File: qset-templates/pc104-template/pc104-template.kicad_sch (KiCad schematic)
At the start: 8 parts

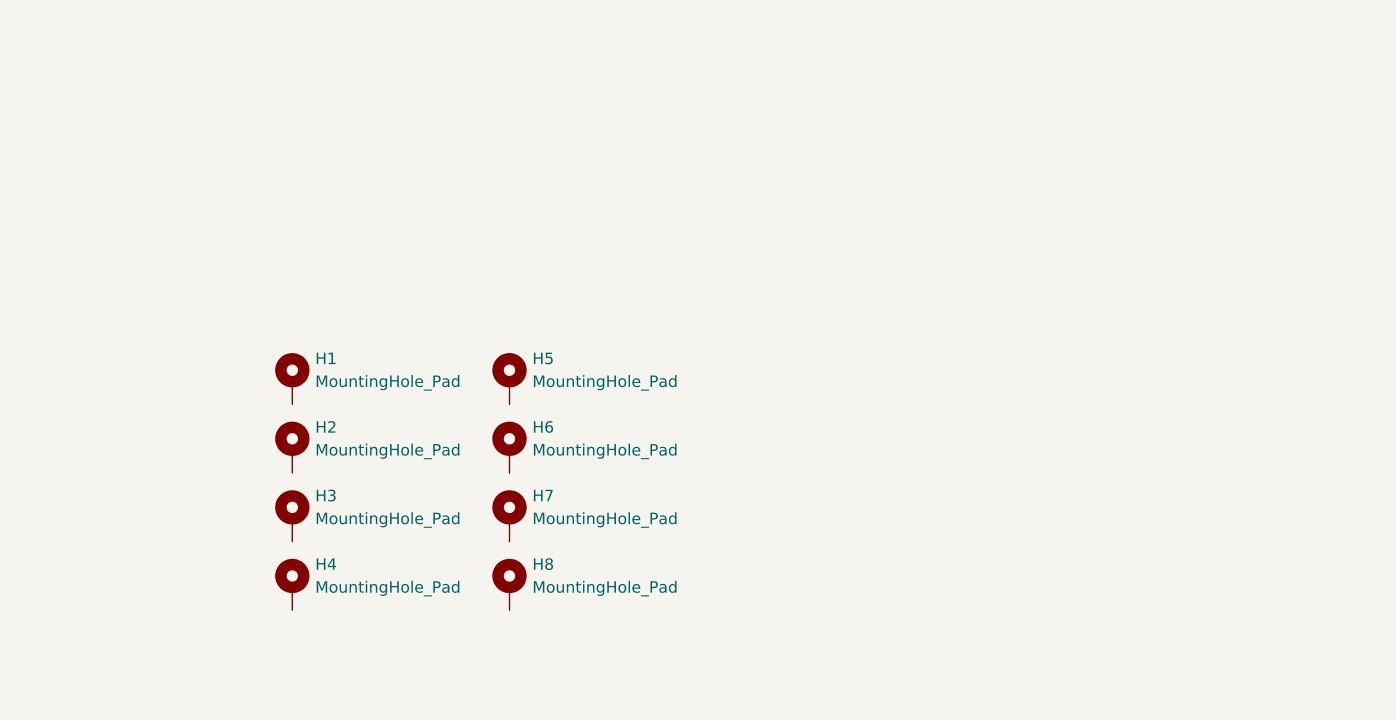
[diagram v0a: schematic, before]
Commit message: templates: pc104: complete template with MH, PC104, and edges
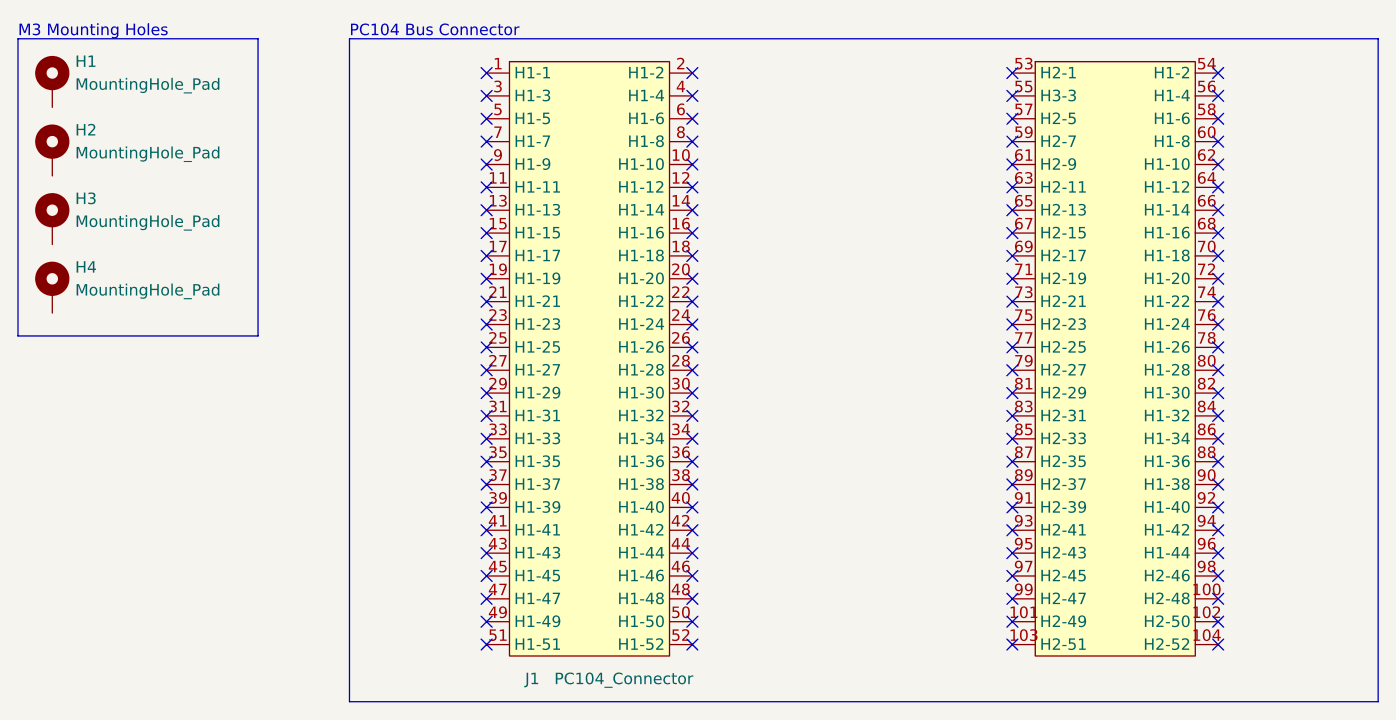
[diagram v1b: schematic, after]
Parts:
- removed H5, H6, H7, H8: MountingHole_Pad, MountingHole:MountingHole_3.2mm_M3_Pad_TopBottom, symbol Mechanical:MountingHole_Pad
- added J1: PC104_Connector, pc104-connector:pc104-connector, symbol qset-connector-library:PC104_Connector
- H1: footprint (none) -> MountingHole:MountingHole_3.2mm_M3_Pad_TopBottom
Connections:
- no-connect marks 0 -> 104
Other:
- note added: "M3 Mounting Holes"
- note added: "PC104 Bus Connector"
- moved on the sheet: H1, H2, H3, H4

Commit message: templates: pc104: include cutouts on all 4 edges
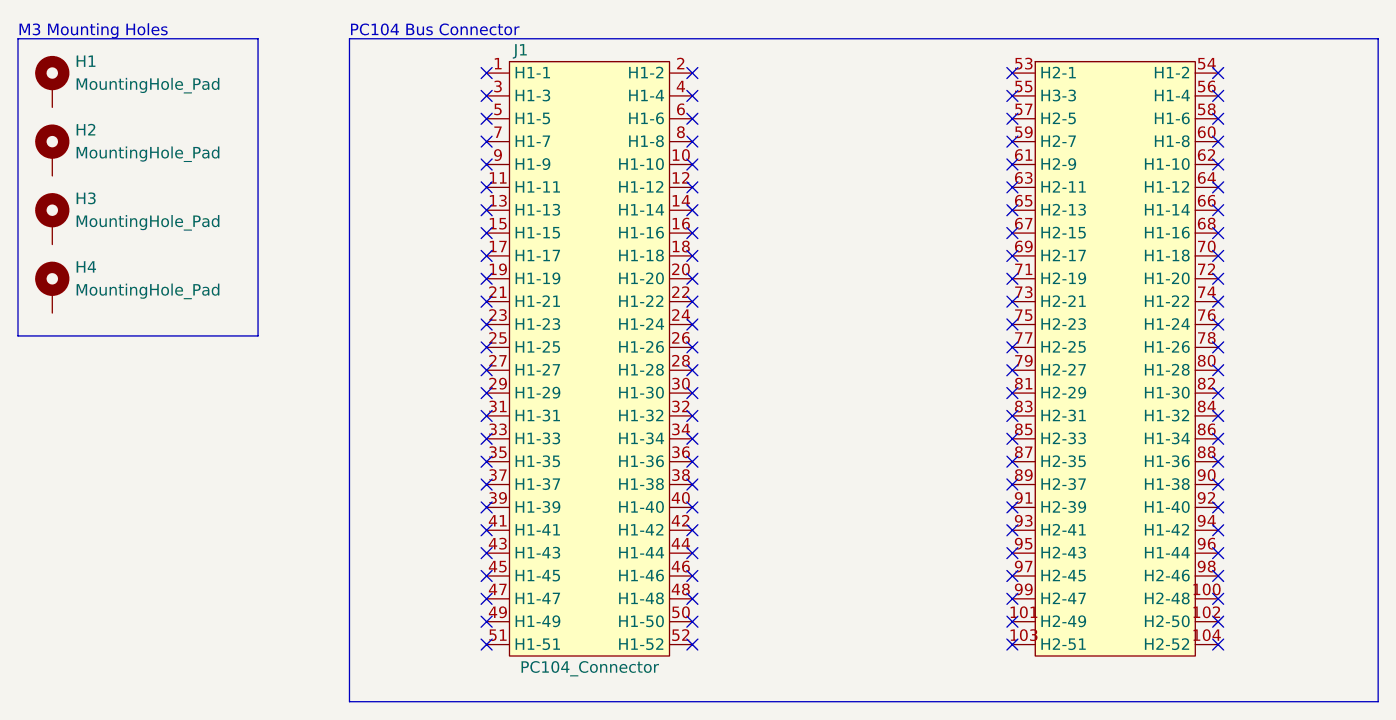
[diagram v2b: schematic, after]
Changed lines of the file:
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@@
   (symbol (lib_id "qset-connector-library:PC104_Connector") (at 106.68 15.24 0) (unit 1)
     (in_bom yes) (on_board yes)
-    (property "Reference" "J1" (id 0) (at 71.12 86.36 0))
-    (property "Value" "PC104_Connector" (id 1) (at 81.28 86.36 0))
+    (property "Reference" "J1" (id 0) (at 69.85 16.51 0))
+    (property "Value" "PC104_Connector" (id 1) (at 77.47 85.09 0))
     (property "Footprint" "pc104-connector:pc104-connector" (id 2) (at 78.74 13.97 0)
       (effects (font (size 1.27 1.27)) hide)
